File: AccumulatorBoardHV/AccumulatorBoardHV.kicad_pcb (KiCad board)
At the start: 2 copper layers, 154.3 x 69.2 mm, 49 parts, among them J1 TS -> GLV Regulator Jumper, J2 To LV Board, J3 Batt Voltage, J4 TS (Switched), J5 IMD TS, J6 To LV Board, J7 Acc LED 1, J8 Acc LED 2, J9 Charger Current, Q1 Q_NMOS_GDS, U1 V110C12E100BL, U2 DK1A1B-12V, U3 RDD08110S3V3, U4 PS2501-1, U5 PS2501-1, U6 G2RL-1A-E, U7 G2RL-1A-E

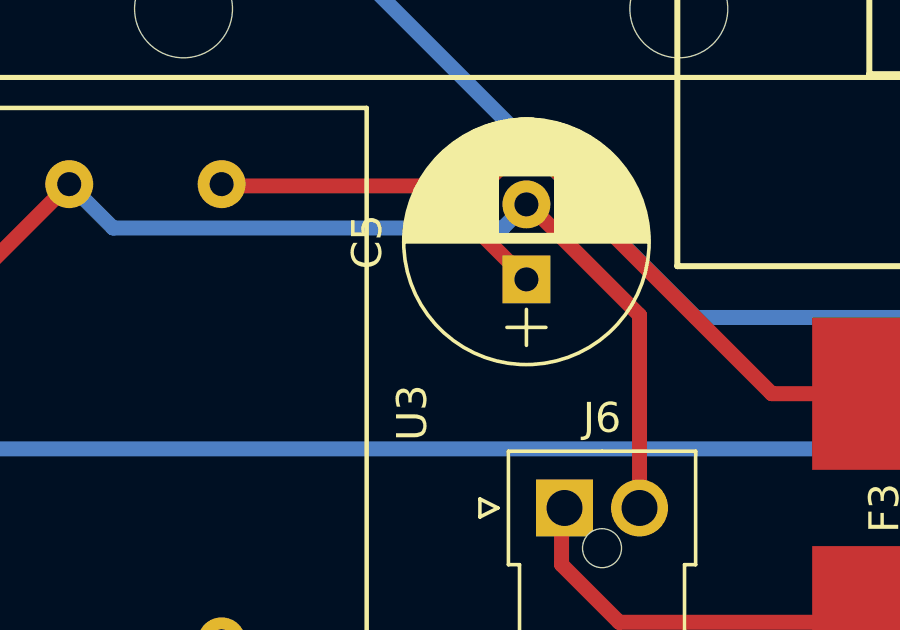
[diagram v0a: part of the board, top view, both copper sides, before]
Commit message: Edit some component labels and other items for PCB send out
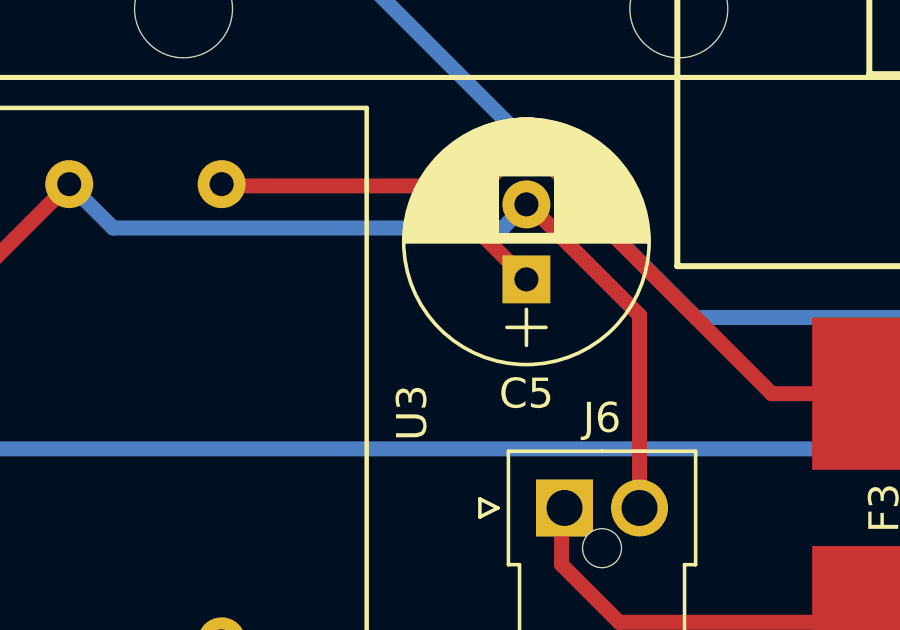
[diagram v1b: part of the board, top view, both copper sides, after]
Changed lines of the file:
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@@
     (links 81)
     (no_connects 0)
-    (area 23.444999 31.064999 177.850001 100.380001)
+    (area 21.3 30.419999 180.095 102.205)
     (thickness 1.6)
     (drawings 38)
@@
     (descr "CP, Radial series, Radial, pin pitch=2.50mm, , diameter=8mm, Electrolytic Capacitor")
     (tags "CP Radial series Radial pin pitch 2.50mm  diameter 8mm Electrolytic Capacitor")
-    (fp_text reference C5 (at 1.25 -5.31 90) (layer F.SilkS)
+    (fp_text reference C5 (at -3.81 0 180) (layer F.SilkS)
       (effects (font (size 1 1) (thickness 0.15)))
     )
@@
   (segment (start 88.265 62.23) (end 85.2055 62.23) (width 0.25) (layer F.Cu) (net 31))
   (segment (start 77.30465 77.43165) (end 77.30465 80.55635) (width 0.25) (layer F.Cu) (net 32))
-  (segment (start 52.07 86.36) (end 47.371 81.661) (width 0.25) (layer F.Cu) (net 32) (status 800000))
+  (segment (start 52.07 86.36) (end 47.371 81.661) (width 0.25) (layer F.Cu) (net 32))
   (segment (start 71.501 86.36) (end 52.07 86.36) (width 0.25) (layer F.Cu) (net 32))
   (segment (start 77.30465 80.55635) (end 71.501 86.36) (width 0.25) (layer F.Cu) (net 32))
